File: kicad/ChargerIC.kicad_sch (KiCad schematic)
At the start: 58 parts, among them J2 I2C, Q1 CSD17575Q3, U1 BQ24179YBGR, U2 MM3Z13VT1G, U3 MM3Z13VT1G, U4 MCP1804x-3002xOT

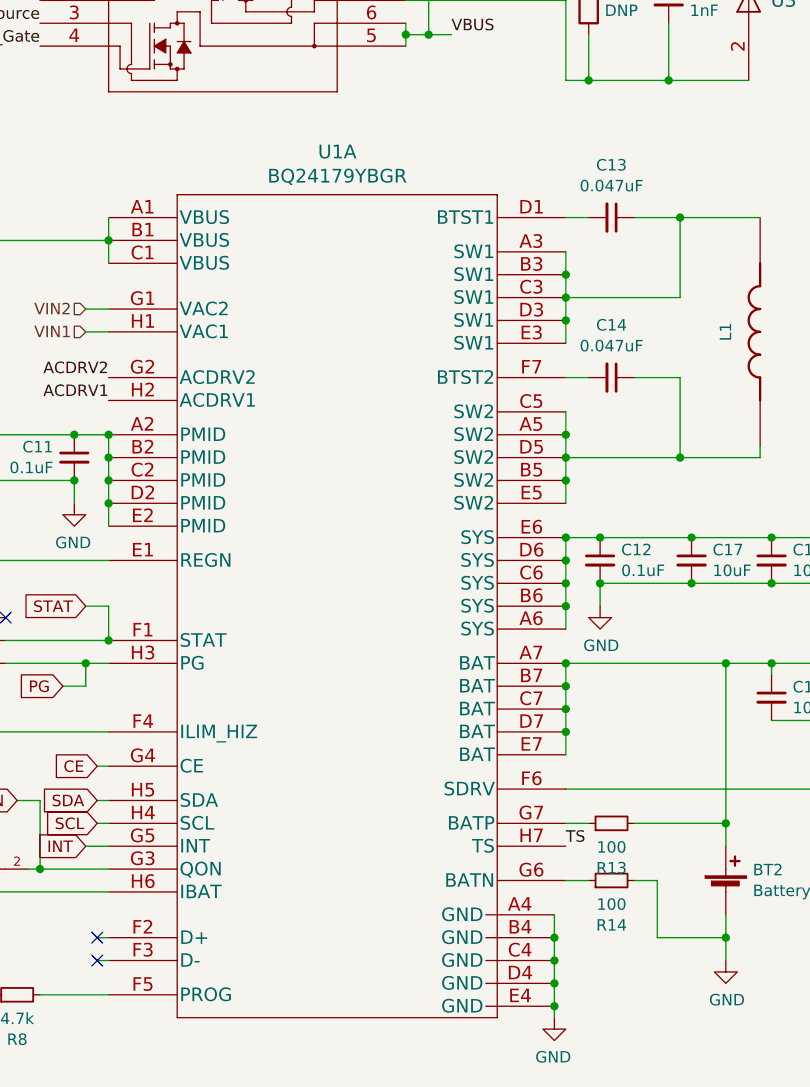
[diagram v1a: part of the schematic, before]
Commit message: Removed duplicate pins on ChargerIC.kicad_sch
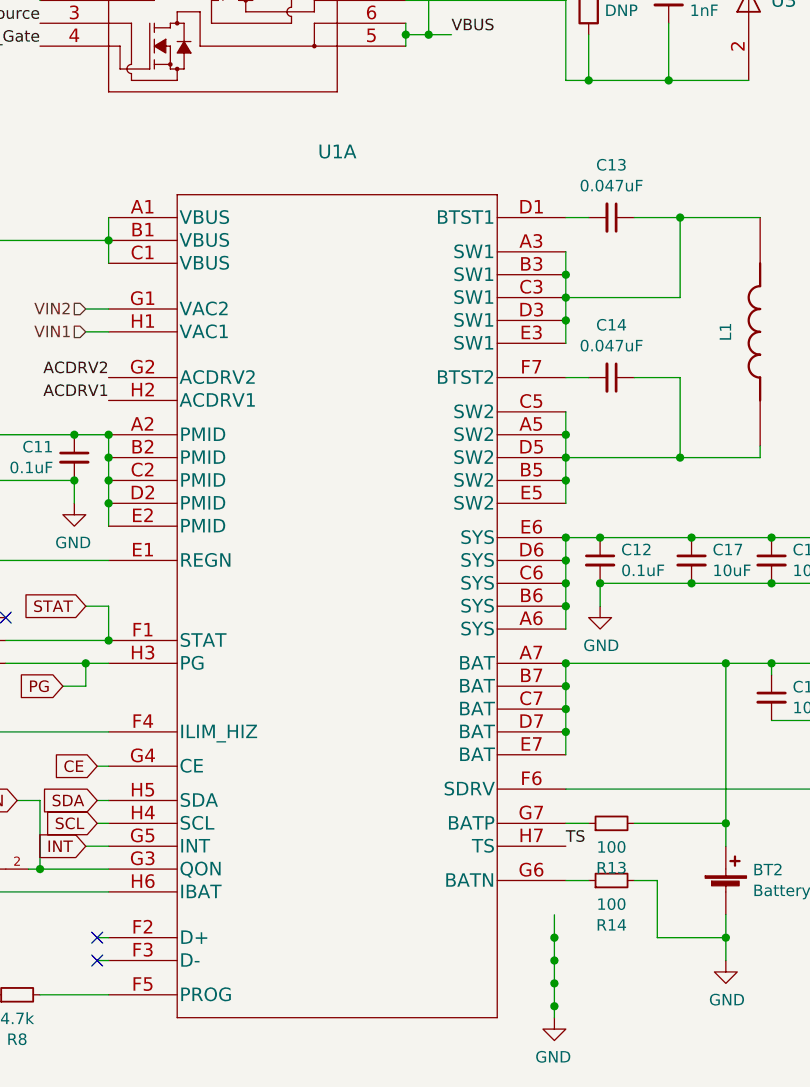
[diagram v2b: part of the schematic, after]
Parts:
- U1: value BQ24179YBGR -> (none); footprint custom_modules:BQ24179YBGR -> (none)
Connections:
- net GND: no longer U1.A4 (GND), U1.B4 (GND), U1.C4 (GND), U1.D4 (GND), U1.E4 (GND)
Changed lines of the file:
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@@
       (effects (font (size 1.524 1.524)))
     )
-    (property "Value" "BQ24179YBGR" (id 1) (at 118.11 93.1926 0)
+    (property "Value" "" (id 1) (at 118.11 93.1926 0)
       (effects (font (size 1.524 1.524)))
     )
-    (property "Footprint" "custom_modules:BQ24179YBGR" (id 2) (at 118.11 94.234 0)
+    (property "Footprint" "" (id 2) (at 118.11 94.234 0)
       (effects (font (size 1.524 1.524)) hide)
     )
@@
     (pin "A2")
     (pin "A3")
-    (pin "A4")
     (pin "A5")
     (pin "A6")
@@
     (pin "B2")
     (pin "B3")
-    (pin "B4")
     (pin "B5")
     (pin "B6")
@@
     (pin "C2")
     (pin "C3")
-    (pin "C4")
     (pin "C5")
     (pin "C6")
@@
     (pin "D2")
     (pin "D3")
-    (pin "D4")
     (pin "D5")
     (pin "D6")
@@
     (pin "E2")
     (pin "E3")
-    (pin "E4")
     (pin "E5")
     (pin "E6")

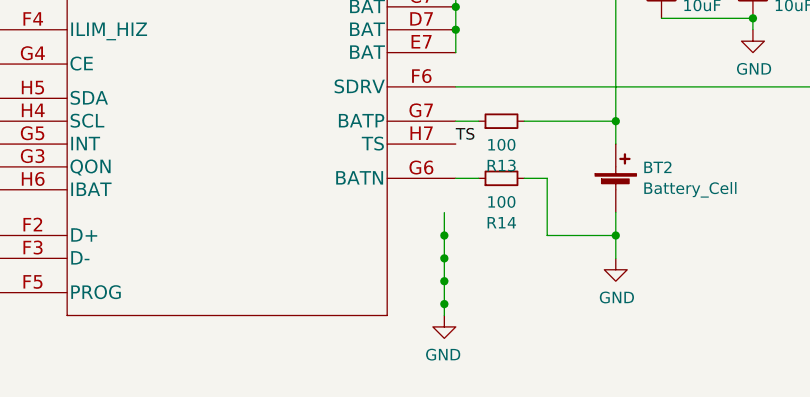
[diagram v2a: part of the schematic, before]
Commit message: Showed and moved hidden GND pins
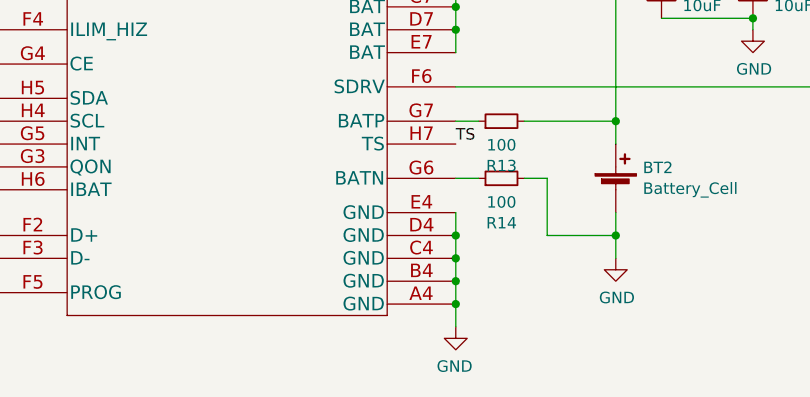
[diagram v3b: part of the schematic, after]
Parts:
- U1: footprint (none) -> custom_modules:BQ24179YBGR
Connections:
- net GND: now also U1.A4 (GND), U1.B4 (GND), U1.C4 (GND), U1.D4 (GND), U1.E4 (GND)
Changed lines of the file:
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@@
   (junction (at 143.51 140.97) (diameter 0) (color 0 0 0 0)
   )
+  (junction (at 143.51 177.8) (diameter 0) (color 0 0 0 0)
+  )
   (junction (at 176.53 153.67) (diameter 0) (color 0 0 0 0)
   )
@@
   (junction (at 161.29 147.32) (diameter 0) (color 0 0 0 0)
   )
+  (junction (at 143.51 180.34) (diameter 0) (color 0 0 0 0)
+  )
   (junction (at 175.26 133.35) (diameter 0) (color 0 0 0 0)
   )
@@
   (junction (at 60.96 121.92) (diameter 0) (color 0 0 0 0)
   )
-  (junction (at 142.24 182.88) (diameter 0) (color 0 0 0 0)
-  )
-  (junction (at 142.24 185.42) (diameter 0) (color 0 0 0 0)
+  (junction (at 143.51 185.42) (diameter 0) (color 0 0 0 0)
   )
   (junction (at 143.51 149.86) (diameter 0) (color 0 0 0 0)
@@
   (junction (at 88.9 121.92) (diameter 0) (color 0 0 0 0)
   )
+  (junction (at 143.51 182.88) (diameter 0) (color 0 0 0 0)
+  )
   (junction (at 146.05 46.99) (diameter 0) (color 0 0 0 0)
   )
@@
   (junction (at 143.51 124.46) (diameter 0) (color 0 0 0 0)
   )
-  (junction (at 142.24 177.8) (diameter 0) (color 0 0 0 0)
-  )
   (junction (at 143.51 133.35) (diameter 0) (color 0 0 0 0)
   )
@@
   )
   (junction (at 184.15 138.43) (diameter 0) (color 0 0 0 0)
-  )
-  (junction (at 142.24 180.34) (diameter 0) (color 0 0 0 0)
   )
   (junction (at 143.51 138.43) (diameter 0) (color 0 0 0 0)
@@
     (stroke (width 0) (type default) (color 0 0 0 0))
   )
-  (wire (pts (xy 142.24 180.34) (xy 142.24 182.88))
-    (stroke (width 0) (type default) (color 0 0 0 0))
-  )
   (wire (pts (xy 166.37 133.35) (xy 175.26 133.35))
     (stroke (width 0) (type default) (color 0 0 0 0))
@@
     (stroke (width 0) (type default) (color 0 0 0 0))
   )
-  (wire (pts (xy 142.24 175.26) (xy 142.24 177.8))
+  (wire (pts (xy 143.51 175.26) (xy 143.51 177.8))
     (stroke (width 0) (type default) (color 0 0 0 0))
   )
@@
     (stroke (width 0) (type default) (color 0 0 0 0))
   )
+  (wire (pts (xy 143.51 182.88) (xy 143.51 185.42))
+    (stroke (width 0) (type default) (color 0 0 0 0))
+  )
   (wire (pts (xy 143.51 106.68) (xy 143.51 109.22))
     (stroke (width 0) (type default) (color 0 0 0 0))
@@
     (stroke (width 0) (type default) (color 0 0 0 0))
   )
+  (wire (pts (xy 143.51 177.8) (xy 143.51 180.34))
+    (stroke (width 0) (type default) (color 0 0 0 0))
+  )
   (wire (pts (xy 78.74 127) (xy 69.85 127))
     (stroke (width 0) (type default) (color 0 0 0 0))
@@
     (stroke (width 0) (type default) (color 0 0 0 0))
   )
-  (wire (pts (xy 142.24 185.42) (xy 142.24 186.69))
-    (stroke (width 0) (type default) (color 0 0 0 0))
-  )
   (wire (pts (xy 184.15 133.35) (xy 193.04 133.35))
     (stroke (width 0) (type default) (color 0 0 0 0))
@@
     (stroke (width 0) (type default) (color 0 0 0 0))
   )
+  (wire (pts (xy 143.51 185.42) (xy 143.51 187.96))
+    (stroke (width 0) (type default) (color 0 0 0 0))
+  )
   (wire (pts (xy 69.85 121.92) (xy 60.96 121.92))
     (stroke (width 0) (type default) (color 0 0 0 0))
@@
     (stroke (width 0) (type default) (color 0 0 0 0))
   )
-  (wire (pts (xy 142.24 182.88) (xy 142.24 185.42))
-    (stroke (width 0) (type default) (color 0 0 0 0))
-  )
   (wire (pts (xy 76.2 172.72) (xy 80.01 172.72))
     (stroke (width 0) (type default) (color 0 0 0 0))
@@
     (stroke (width 0) (type default) (color 0 0 0 0))
   )
+  (wire (pts (xy 143.51 180.34) (xy 143.51 182.88))
+    (stroke (width 0) (type default) (color 0 0 0 0))
+  )
   (wire (pts (xy 30.48 153.67) (xy 40.64 153.67))
     (stroke (width 0) (type default) (color 0 0 0 0))
@@
   )
   (wire (pts (xy 130.81 41.91) (xy 128.27 41.91))
-    (stroke (width 0) (type default) (color 0 0 0 0))
-  )
-  (wire (pts (xy 142.24 177.8) (xy 142.24 180.34))
     (stroke (width 0) (type default) (color 0 0 0 0))
   )
@@
       (effects (font (size 1.524 1.524)))
     )
-    (property "Footprint" "" (id 2) (at 118.11 94.234 0)
+    (property "Footprint" "custom_modules:BQ24179YBGR" (id 2) (at 118.11 94.234 0)
       (effects (font (size 1.524 1.524)) hide)
     )
@@
     (pin "A2")
     (pin "A3")
+    (pin "A4")
     (pin "A5")
     (pin "A6")
@@
     (pin "B2")
     (pin "B3")
+    (pin "B4")
     (pin "B5")
     (pin "B6")
@@
     (pin "C2")
     (pin "C3")
+    (pin "C4")
     (pin "C5")
     (pin "C6")
@@
     (pin "D2")
     (pin "D3")
+    (pin "D4")
     (pin "D5")
     (pin "D6")
@@
     (pin "E2")
     (pin "E3")
+    (pin "E4")
     (pin "E5")
     (pin "E6")
@@
     (pin "H6")
     (pin "H7")
-    (pin "A4")
-    (pin "B4")
-    (pin "C4")
-    (pin "D4")
-    (pin "E4")
   )
   (symbol (lib_id "robot-rescue:AON7810-AON7810") (at 85.09 35.56 0) (unit 1)
@@
     (pin "1")
   )
-  (symbol (lib_id "robot-rescue:GND-power") (at 142.24 186.69 0) (mirror y) (unit 1)
-    (in_bom yes) (on_board yes)
-    (property "Reference" "#PWR0103" (id 0) (at 142.24 193.04 0)
-      (effects (font (size 1.27 1.27)) hide)
-    )
-    (property "Value" "GND" (id 1) (at 142.113 191.0842 0))
-    (property "Footprint" "" (id 2) (at 142.24 186.69 0)
-      (effects (font (size 1.27 1.27)) hide)
-    )
-    (property "Datasheet" "" (id 3) (at 142.24 186.69 0)
-      (effects (font (size 1.27 1.27)) hide)
-    )
+  (symbol (lib_id "robot-rescue:GND-power") (at 143.51 187.96 0) (mirror y) (unit 1)
+    (in_bom yes) (on_board yes)
+    (property "Reference" "#PWR0103" (id 0) (at 143.51 194.31 0)
+      (effects (font (size 1.27 1.27)) hide)
+    )
+    (property "Value" "GND" (id 1) (at 143.383 192.3542 0))
+    (property "Footprint" "" (id 2) (at 143.51 187.96 0)
+      (effects (font (size 1.27 1.27)) hide)
+    )
+    (property "Datasheet" "" (id 3) (at 143.51 187.96 0)
+      (effects (font (size 1.27 1.27)) hide)
+    )

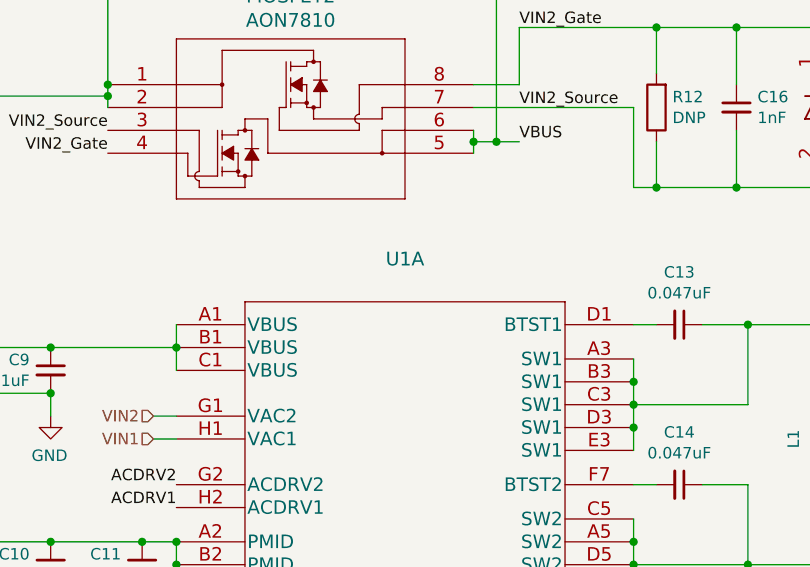
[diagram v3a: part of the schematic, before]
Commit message: Value added to ChargerIC
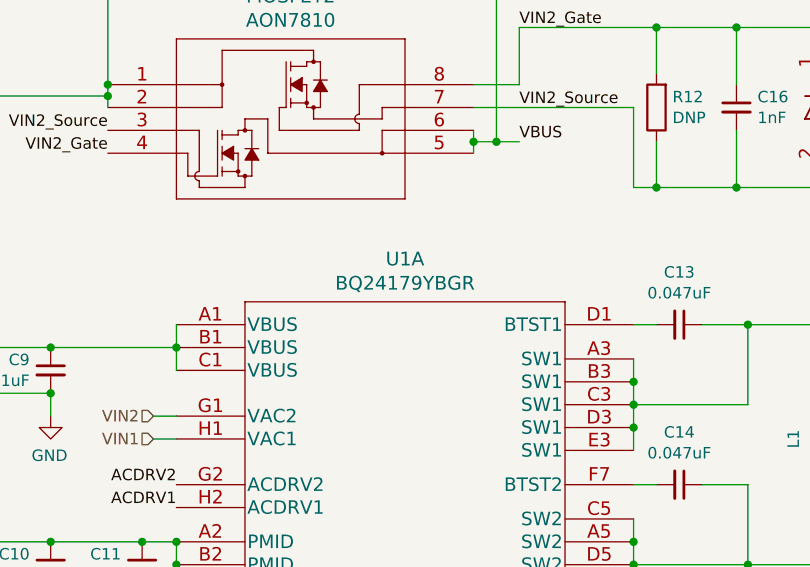
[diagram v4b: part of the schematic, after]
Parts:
- U1: value (none) -> BQ24179YBGR
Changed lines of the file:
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@@
       (effects (font (size 1.524 1.524)))
     )
-    (property "Value" "" (id 1) (at 118.11 93.1926 0)
+    (property "Value" "BQ24179YBGR" (id 1) (at 118.11 93.1926 0)
       (effects (font (size 1.524 1.524)))
     )
